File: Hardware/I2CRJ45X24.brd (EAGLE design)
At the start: 216 x 50 mm, 127 parts, among them IC1 MCP23017SO, IC2 MCP23017SO, IC3 MCP23017SO, IC4 MCP23017SO, IC5 MCP23017SO, IC6 MCP23017SO, J1 RJ45-X8, J2 RJ45-X8, J3 RJ45-X8, J4 I2C-BREAKOUT, J5 M01-PLAIN, J9 I2C-BREAKOUT

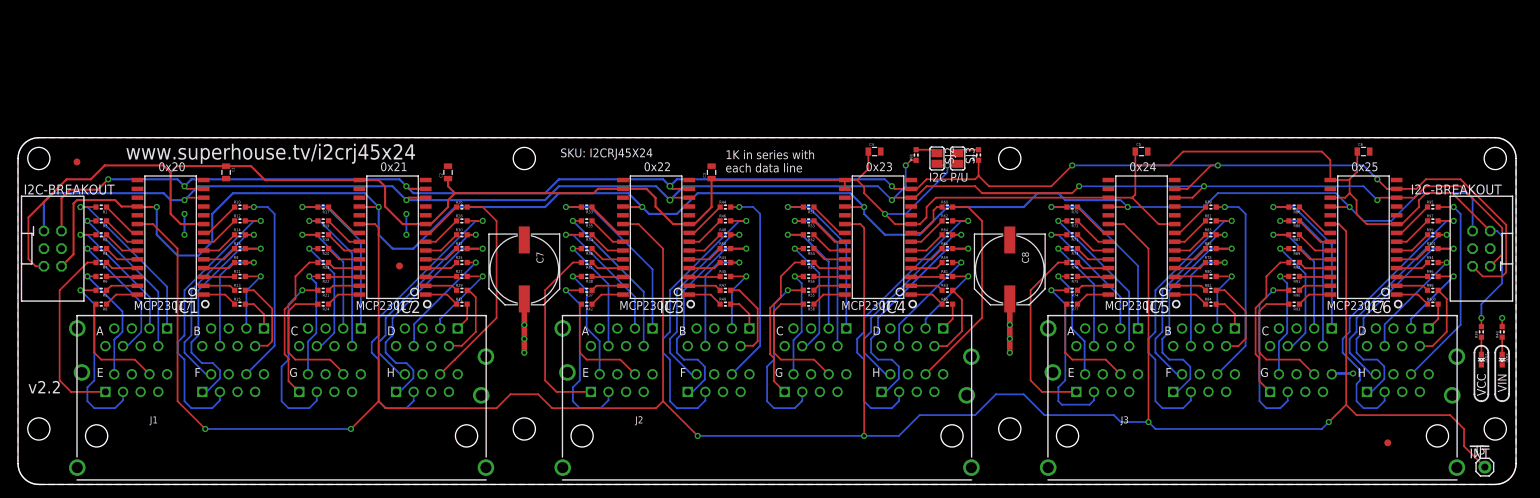
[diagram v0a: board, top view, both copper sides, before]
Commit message: Renumbered parts to optimise production.
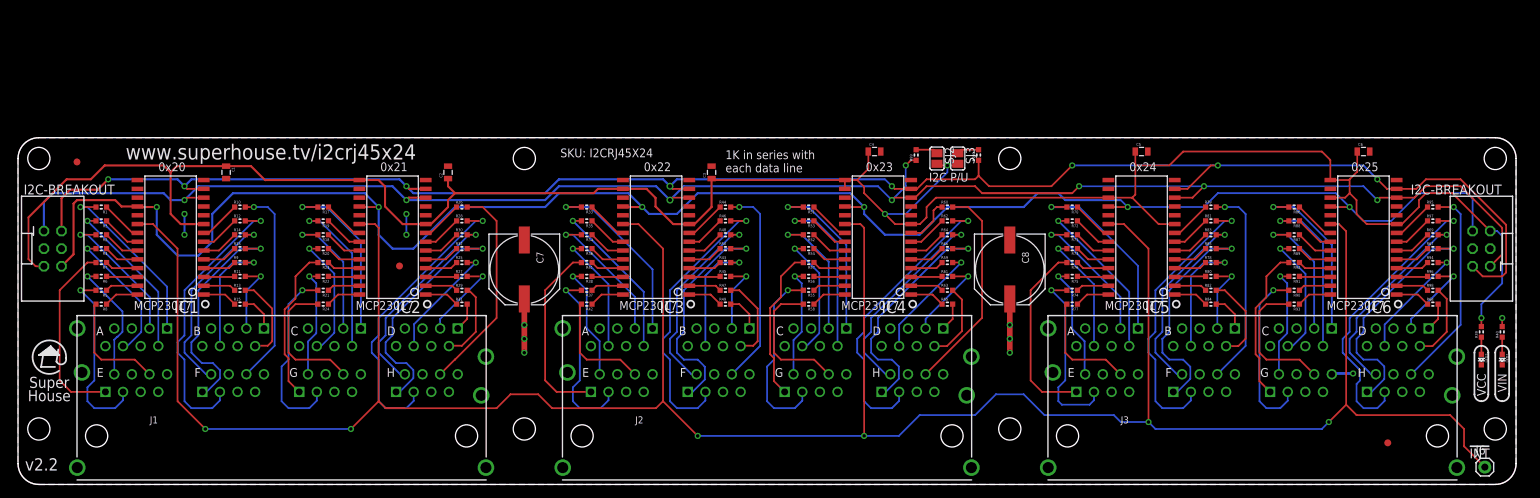
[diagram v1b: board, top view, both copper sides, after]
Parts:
- removed J9: I2C-BREAKOUT, SuperHouse-Connectors:2X03-SHROUDED
- added J6: M01-PLAIN, SuperHouse-Connectors:1X01
- J5: value M01-PLAIN -> I2C-BREAKOUT; device SuperHouse-Connectors:1X01 -> SuperHouse-Connectors:2X03-SHROUDED
- R100, R99: value 1K -> 4K7
- R68, R69: value 4K7 -> 1K
- moved R68 77.5 mm to (204.0, 26.0), turned to 0 degrees
- moved R99 75.4 mm to (129.5, 47.5), turned to 90 degrees
- moved R100 68.9 mm to (138.5, 47.5), turned to 90 degrees
- moved R69 66.5 mm to (204.0, 36.0), turned to 0 degrees
- moved J5 31.5 mm to (211.0, 34.0), turned to 180 degrees
- renumbered LED3 to LED1, R101 to R67
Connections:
- net !INT: now also J6.1; no longer J5.1
- net !RESET: now also J5.6; no longer J9.6
- net 3D1: now also R68.2; no longer R100.2
- net 3H2: now also R69.2; no longer R99.2
- net GND: now also J5.4; no longer J9.4
- net GPB0-6: now also R68.1; no longer R100.1
- net GPB5-6: now also R69.1; no longer R99.1
- net N$1: now also R99.2; no longer R68.2
- net N$2: now also R100.2; no longer R69.2
- net SCL: now also J5.1, R99.1; no longer J9.1, R68.1
- net SDA: now also J5.2, R100.1; no longer J9.2, R69.1
- net VCC: now also J5.5; no longer J9.5
- net VIN: now also J5.3; no longer J9.3
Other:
- board text added: "24-Channel I2C RJ45 Breakout"
- board text removed: "24 Channel I2C RJ45 Breakout"

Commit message: Major clean-up in preparation for recreating x8 and x16 versions based on the x24 version. Moved rear silkscreen into left third. Increased size of all data traces. Improved bottom power plane pour. Changed LED resistors to 4K7.
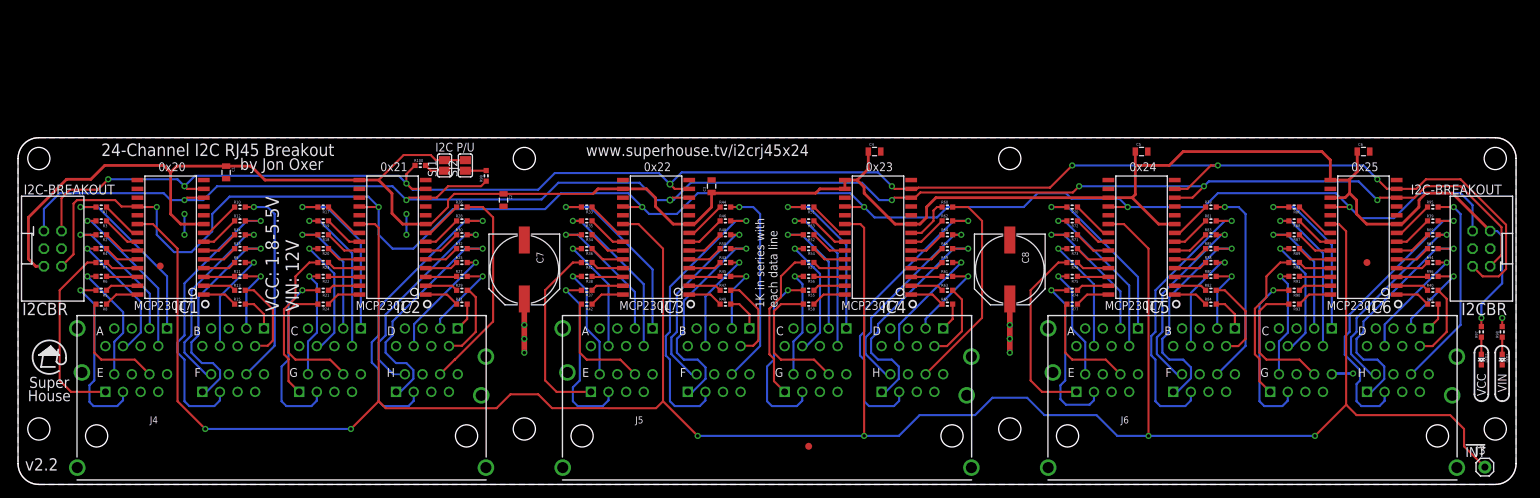
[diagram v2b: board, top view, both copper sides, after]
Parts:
- removed SJ3: SDA PU, SuperHouse-Jumpers:SJ
- added SJ1: SDA PU, SuperHouse-Jumpers:SJ
- J1, J2: value RJ45-X8 -> I2C-BREAKOUT; device SuperHouse-Connectors:RJ45-2X4 -> SuperHouse-Connectors:2X03-SHROUDED
- J3: value RJ45-X8 -> M01-PLAIN; device SuperHouse-Connectors:RJ45-2X4 -> SuperHouse-Connectors:1X01
- J4, J5: value I2C-BREAKOUT -> RJ45-X8; device SuperHouse-Connectors:2X03-SHROUDED -> SuperHouse-Connectors:RJ45-2X4
- J6: value M01-PLAIN -> RJ45-X8; device SuperHouse-Connectors:1X01 -> SuperHouse-Connectors:RJ45-2X4
- R39, R40: value 2K2 -> 1K
- R97, R98: value 1K -> 4K7
- moved J2 106.5 mm to (211.0, 34.0), turned to 180 degrees
- moved J5 106.5 mm to (108.0, 7.00), turned to 0 degrees
- moved R100 80.5 mm to (58.0, 46.0), turned to 0 degrees
- moved SJ2 68.0 mm to (64.5, 46.0), turned to 90 degrees
- moved FID3 64.5 mm to (114.0, 5.50)
- moved R99 62.1 mm to (67.5, 44.5)
- moved J1 42.6 mm to (5.00, 34.0)
- moved J4 42.6 mm to (38.0, 7.00)
- moved J3 33.8 mm to (211.5, 2.50)
- moved J6 33.8 mm to (178.0, 7.00)
- moved FID2 26.2 mm to (194.5, 32.0)
- moved FID1 19.2 mm to (20.5, 31.5)
- moved R39 17.5 mm to (204.0, 38.0), turned to 0 degrees
- moved R97 17.5 mm to (211.0, 22.0), turned to 90 degrees
- moved R40 11.7 mm to (204.0, 28.0), turned to 0 degrees
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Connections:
- net !INT: now also J3.1; no longer J6.1
- net !RESET: now also J1.6, J2.6; no longer J4.6, J5.6
- net 1A1: now also J4.A1; no longer J1.A1
- net 1A2: now also J4.A2; no longer J1.A2
- net 1A3: now also J4.A3; no longer J1.A3
- net 1A6: now also J4.A6; no longer J1.A6
- net 1B1: now also J4.B1; no longer J1.B1
- net 1B2: now also J4.B2; no longer J1.B2
- net 1B3: now also J4.B3; no longer J1.B3
- net 1B6: now also J4.B6; no longer J1.B6
- net 1C1: now also J4.C1; no longer J1.C1
- net 1C2: now also J4.C2; no longer J1.C2
- net 1C3: now also J4.C3; no longer J1.C3
- net 1C6: now also J4.C6; no longer J1.C6
- net 1D1: now also J4.D1; no longer J1.D1
- net 1D2: now also J4.D2; no longer J1.D2
- net 1D3: now also J4.D3; no longer J1.D3
- net 1D6: now also J4.D6; no longer J1.D6
- net 1E1: now also J4.E1; no longer J1.E1
- net 1E2: now also J4.E2; no longer J1.E2
- net 1E3: now also J4.E3; no longer J1.E3
- net 1E6: now also J4.E6; no longer J1.E6
- net 1F1: now also J4.F1; no longer J1.F1
- net 1F2: now also J4.F2; no longer J1.F2
- net 1F3: now also J4.F3; no longer J1.F3
- net 1F6: now also J4.F6; no longer J1.F6
- net 1G1: now also J4.G1; no longer J1.G1
- net 1G2: now also J4.G2; no longer J1.G2
- net 1G3: now also J4.G3; no longer J1.G3
- net 1G6: now also J4.G6; no longer J1.G6
- net 1H1: now also J4.H1; no longer J1.H1
- net 1H2: now also J4.H2; no longer J1.H2
- net 1H3: now also J4.H3; no longer J1.H3
- net 1H6: now also J4.H6; no longer J1.H6
- net 2A1: now also J5.A1; no longer J2.A1
- net 2A2: now also J5.A2; no longer J2.A2
- net 2A3: now also J5.A3; no longer J2.A3
- net 2A6: now also J5.A6; no longer J2.A6
- net 2B1: now also J5.B1; no longer J2.B1
- net 2B2: now also J5.B2; no longer J2.B2
- net 2B3: now also J5.B3; no longer J2.B3
- net 2B6: now also J5.B6; no longer J2.B6
- net 2C1: now also J5.C1; no longer J2.C1
- net 2C2: now also J5.C2; no longer J2.C2
- net 2C3: now also J5.C3; no longer J2.C3
- net 2C6: now also J5.C6; no longer J2.C6
- net 2D1: now also J5.D1; no longer J2.D1
- net 2D2: now also J5.D2; no longer J2.D2
- net 2D3: now also J5.D3; no longer J2.D3
- net 2D6: now also J5.D6; no longer J2.D6
- net 2E1: now also J5.E1; no longer J2.E1
- net 2E2: now also J5.E2; no longer J2.E2
- net 2E3: now also J5.E3; no longer J2.E3
- net 2E6: now also J5.E6; no longer J2.E6
- net 2F1: now also J5.F1; no longer J2.F1
- net 2F2: now also J5.F2; no longer J2.F2
- net 2F3: now also J5.F3; no longer J2.F3
- net 2F6: now also J5.F6; no longer J2.F6
- net 2G1: now also J5.G1; no longer J2.G1
- net 2G2: now also J5.G2; no longer J2.G2
- net 2G3: now also J5.G3; no longer J2.G3
- net 2G6: now also J5.G6; no longer J2.G6
- net 2H1: now also J5.H1; no longer J2.H1
- net 2H2: now also J5.H2; no longer J2.H2
- net 2H3: now also J5.H3; no longer J2.H3
- net 2H6: now also J5.H6; no longer J2.H6
- net 3A1: now also J6.A1; no longer J3.A1
- net 3A2: now also J6.A2; no longer J3.A2
- net 3A3: now also J6.A3; no longer J3.A3
- net 3A6: now also J6.A6; no longer J3.A6
- net 3B1: now also J6.B1; no longer J3.B1
- net 3B2: now also J6.B2; no longer J3.B2
- net 3B3: now also J6.B3; no longer J3.B3
- net 3B6: now also J6.B6; no longer J3.B6
- net 3C1: now also J6.C1; no longer J3.C1
- net 3C2: now also J6.C2; no longer J3.C2
- net 3C3: now also J6.C3; no longer J3.C3
- net 3C6: now also J6.C6; no longer J3.C6
- net 3D1: now also J6.D1; no longer J3.D1
- net 3D2: now also J6.D2, R40.2; no longer J3.D2, R98.2
- net 3D3: now also J6.D3; no longer J3.D3
- net 3D6: now also J6.D6; no longer J3.D6
- net 3E1: now also J6.E1; no longer J3.E1
- net 3E2: now also J6.E2; no longer J3.E2
- net 3E3: now also J6.E3; no longer J3.E3
- net 3E6: now also J6.E6; no longer J3.E6
- net 3F1: now also J6.F1; no longer J3.F1
- net 3F2: now also J6.F2; no longer J3.F2
- net 3F3: now also J6.F3; no longer J3.F3
- net 3F6: now also J6.F6; no longer J3.F6
- net 3G1: now also J6.G1; no longer J3.G1
- net 3G2: now also J6.G2; no longer J3.G2
- net 3G3: now also J6.G3; no longer J3.G3
- net 3G6: now also J6.G6; no longer J3.G6
- net 3H1: now also J6.H1; no longer J3.H1
- net 3H2: now also J6.H2; no longer J3.H2
- net 3H3: now also J6.H3, R39.2; no longer J3.H3, R97.2
- net 3H6: now also J6.H6; no longer J3.H6
- net GND: now also J1.4, J2.4, J4.A7, J4.A8, J4.B7, J4.B8, J4.C7, J4.C8, J4.D7, J4.D8, J4.E7, J4.E8, J4.F7, J4.F8, J4.G7, J4.G8, J4.GND0, J4.GND1, J4.GND2, J4.GND3, J4.GND4, J4.GND5, J4.H7, J4.H8, J5.A7, J5.A8, J5.B7, J5.B8, J5.C7, J5.C8, J5.D7, J5.D8, J5.E7, J5.E8, J5.F7, J5.F8, J5.G7, J5.G8, J5.GND0, J5.GND1, J5.GND2, J5.GND3, J5.GND4, J5.GND5, J5.H7, J5.H8, J6.A7, J6.A8, J6.B7, J6.B8, J6.C7, J6.C8, J6.D7, J6.D8, J6.E7, J6.E8, J6.F7, J6.F8, J6.G7, J6.G8, J6.GND0, J6.GND1, J6.GND2, J6.GND3, J6.GND4, J6.GND5, J6.H7, J6.H8; no longer J1.A7, J1.A8, J1.B7, J1.B8, J1.C7, J1.C8, J1.D7, J1.D8, J1.E7, J1.E8, J1.F7, J1.F8, J1.G7, J1.G8, J1.GND0, J1.GND1, J1.GND2, J1.GND3, J1.GND4, J1.GND5, J1.H7, J1.H8, J2.A7, J2.A8, J2.B7, J2.B8, J2.C7, J2.C8, J2.D7, J2.D8, J2.E7, J2.E8, J2.F7, J2.F8, J2.G7, J2.G8, J2.GND0, J2.GND1, J2.GND2, J2.GND3, J2.GND4, J2.GND5, J2.H7, J2.H8, J3.A7, J3.A8, J3.B7, J3.B8, J3.C7, J3.C8, J3.D7, J3.D8, J3.E7, J3.E8, J3.F7, J3.F8, J3.G7, J3.G8, J3.GND0, J3.GND1, J3.GND2, J3.GND3, J3.GND4, J3.GND5, J3.H7, J3.H8, J4.4, J5.4
- net GPB1-6: now also R40.1; no longer R98.1
- net GPB6-6: now also R39.1; no longer R97.1
- net N$2: now also SJ1.1; no longer SJ3.1
- net N$7: now also R97.1; no longer R39.1
- net N$8: now also R98.1; no longer R40.1
- net SCL: now also J1.1, J2.1; no longer J4.1, J5.1
- net SDA: now also J1.2, J2.2; no longer J4.2, J5.2
- net VCC: now also J1.5, J2.5, R97.2, SJ1.2; no longer J4.5, J5.5, R39.2, SJ3.2
- net VIN: now also J1.3, J2.3, J4.A4, J4.A5, J4.B4, J4.B5, J4.C4, J4.C5, J4.D4, J4.D5, J4.E4, J4.E5, J4.F4, J4.F5, J4.G4, J4.G5, J4.H4, J4.H5, J5.A4, J5.A5, J5.B4, J5.B5, J5.C4, J5.C5, J5.D4, J5.D5, J5.E4, J5.E5, J5.F4, J5.F5, J5.G4, J5.G5, J5.H4, J5.H5, J6.A4, J6.A5, J6.B4, J6.B5, J6.C4, J6.C5, J6.D4, J6.D5, J6.E4, J6.E5, J6.F4, J6.F5, J6.G4, J6.G5, J6.H4, J6.H5, R98.2; no longer J1.A4, J1.A5, J1.B4, J1.B5, J1.C4, J1.C5, J1.D4, J1.D5, J1.E4, J1.E5, J1.F4, J1.F5, J1.G4, J1.G5, J1.H4, J1.H5, J2.A4, J2.A5, J2.B4, J2.B5, J2.C4, J2.C5, J2.D4, J2.D5, J2.E4, J2.E5, J2.F4, J2.F5, J2.G4, J2.G5, J2.H4, J2.H5, J3.A4, J3.A5, J3.B4, J3.B5, J3.C4, J3.C5, J3.D4, J3.D5, J3.E4, J3.E5, J3.F4, J3.F5, J3.G4, J3.G5, J3.H4, J3.H5, J4.3, J5.3, R40.2
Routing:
- net VCC: track 332.3 -> 326.7 mm, vias 3 -> 1
- net !RESET: track 264.5 -> 259.2 mm
- net !INT: track 387.0 -> 389.4 mm
- net SCL: track 253.7 -> 255.7 mm, vias 8 -> 7
- net 2B6: track 17.1 -> 15.3 mm
- net 1B6: track 17.1 -> 15.3 mm
- net 3B6: track 17.1 -> 15.6 mm
- net SDA: track 256.6 -> 257.5 mm
- net 3A1: track 27.3 -> 26.3 mm
- net 3C2: track 23.6 -> 22.7 mm
- net 2C2: track 23.6 -> 22.7 mm
- net 1A1: track 25.5 -> 26.4 mm
- net 1H2: track 29.7 -> 30.6 mm
- net 2F1: track 33.0 -> 32.2 mm
- net 2A2: track 23.5 -> 24.2 mm
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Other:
- board text added: "I2CBR"
- board text added: "VCC: 1.8-5.5V VIN: 12V"

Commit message: Added weak pull-up on RESET line.
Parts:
- added R101: 22K, SuperHouse-DiscreteSemi:R0603
- added SJ3: RST-PU, SuperHouse-Jumpers:SJC
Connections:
- new net N$3: R101.2, SJ3.1
- net !RESET: now also R101.1
- net VCC: now also SJ3.2
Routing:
- net N$3: track 0.00 -> 35.8 mm, vias 0 -> 2
- net !RESET: track 259.2 -> 268.4 mm
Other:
- board text added: "RST P/U"
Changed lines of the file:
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@@
 <setting verticaltext="up"/>
 </settings>
-<grid distance="0.1" unitdist="mm" unit="mm" style="lines" multiple="1" display="yes" altdistance="0.005" altunitdist="inch" altunit="inch"/>
+<grid distance="1" unitdist="mm" unit="mm" style="lines" multiple="1" display="yes" altdistance="0.005" altunitdist="inch" altunit="inch"/>
 <layers>
 <layer number="1" name="Top" color="4" fill="1" visible="yes" active="yes"/>
@@
 </layers>
 <board>
-<fusionsync huburn="a.cGVyc29uYWw6dWUyZDliZmNi" projecturn="a.cGVyc29uYWw6dWUyZDliZmNiIzIwMTkwNjE5MTk5NjgzNjgx" f3durn="urn:adsk.wipprod:dm.lineage:7PE12rU6Rs2d8xNWJ3I8mw" pcbguid="240f1cde-c83f-4e3e-9fac-562d2bf45fdf" lastpulledtime="" lastsyncedchangeguid="1491f9b9-a179-9c0a-9821-19275fe4b9b0" latestrevisionid="" lastsyncedrevisionid="" lastboardhashguid="1feeb865-bf47-de78-9034-8c028aa0d644" lastpushedtime="2021-04-15T02:54:13Z" linktopcb3d="false"/>
+<fusionsync huburn="a.cGVyc29uYWw6dWUyZDliZmNi" projecturn="a.cGVyc29uYWw6dWUyZDliZmNiIzIwMTkwNjE5MTk5NjgzNjgx" f3durn="urn:adsk.wipprod:dm.lineage:7PE12rU6Rs2d8xNWJ3I8mw" pcbguid="240f1cde-c83f-4e3e-9fac-562d2bf45fdf" lastpulledtime="" lastsyncedchangeguid="1491f9b9-a179-9c0a-9821-19275fe4b9b0" latestrevisionid="" lastsyncedrevisionid="" lastboardhashguid="57911f44-b240-5674-ec1f-8acbffdfcb08" lastpushedtime="2021-04-15T04:03:47Z" linktopcb3d="false"/>
 <plain>
 <wire x1="3" y1="0" x2="0" y2="3" width="0" layer="20" curve="-90"/>
@@
 <circle x="3" y="47" radius="3.201559375" width="0.254" layer="41"/>
 <circle x="3" y="47" radius="3.201559375" width="0.254" layer="42"/>
-<dimension x1="0" y1="-1" x2="38" y2="-1" x3="19" y3="-9" textsize="1.778" layer="47"/>
-<dimension x1="38" y1="-1" x2="108" y2="-1" x3="73" y3="-9" textsize="1.778" layer="47"/>
-<dimension x1="108" y1="-1" x2="178" y2="-1" x3="143" y3="-9" textsize="1.778" layer="47"/>
+<dimension x1="0" y1="-1" x2="38" y2="-1" x3="19" y3="-7" textsize="1.778" layer="47"/>
+<dimension x1="38" y1="-1" x2="108" y2="-1" x3="73" y3="-7" textsize="1.778" layer="47"/>
+<dimension x1="108" y1="-1" x2="178" y2="-1" x3="143" y3="-7" textsize="1.778" layer="47"/>
 <text x="47.5" y="37.354" size="1.6764" layer="22" font="vector" ratio="17" rot="MR0" align="bottom-center">www.superhouse.tv</text>
 <dimension x1="3" y1="51" x2="73" y2="51" x3="38" y3="52" textsize="1.778" layer="47"/>
@@
 <text x="37.455" y="1.854" size="2.3" layer="22" font="vector" ratio="17" rot="MR0" align="bottom-center">www.superhouse.tv/i2crj45x24</text>
 <text x="4.671" y="11.309" size="1.4224" layer="22" font="vector" ratio="17" rot="MR90">SKU: I2CRJ45X24</text>
+<text x="8.691" y="43.671" size="1.27" layer="21" font="vector" ratio="17" align="bottom-center">RST P/U</text>
+<dimension x1="217" y1="50" x2="217" y2="0" x3="220" y3="25" textsize="1.778" layer="47"/>
+<dimension x1="0" y1="57" x2="216" y2="57" x3="108" y3="58" textsize="1.778" layer="47"/>
+<dimension x1="178" y1="-1" x2="216" y2="-1" x3="197" y3="-7" textsize="1.778" layer="47"/>
 </plain>
 <attributes>
@@
 <attribute name="VALUE" x="214.9652" y="20.984" size="0.4064" layer="27" font="vector" rot="R90"/>
 </element>
+<element name="R101" library="SuperHouse-DiscreteSemi" library_urn="urn:adsk.eagle:library:11768461" package="R0603" package3d_urn="urn:adsk.eagle:package:11768543/2" value="22K" x="3.6" y="23.1" smashed="yes" rot="R180">
+<attribute name="NAME" x="4.489" y="22.592" size="0.4064" layer="25" font="vector" rot="R180"/>
+<attribute name="VALUE" x="4.616" y="24.0652" size="0.4064" layer="27" font="vector" rot="R180"/>
+</element>
+<element name="SJ3" library="SuperHouse-Jumpers" library_urn="urn:adsk.eagle:library:12190622" package="SJC" package3d_urn="urn:adsk.eagle:package:7066342/2" value="RST-PU" x="8.4" y="46.9" smashed="yes" rot="R270">
+<attribute name="NAME" x="9.543" y="48.551" size="1.27" layer="25" ratio="10" rot="R270"/>
+<attribute name="VALUE" x="8.4" y="46.4999" size="0.02" layer="27" rot="R270"/>
+</element>
 </elements>
 <signals>
@@
 <via x="13" y="44" extent="1-16" drill="0.5"/>
 <wire x1="13" y1="44" x2="11.5" y2="42.5" width="0.3048" layer="1"/>
-<wire x1="11.5" y1="42.5" x2="7.5" y2="42.5" width="0.3048" layer="1"/>
-<wire x1="7.5" y1="42.5" x2="6.27" y2="41.27" width="0.3048" layer="1"/>
-<wire x1="6.27" y1="41.27" x2="6.27" y2="36.54" width="0.3048" layer="1"/>
+<wire x1="11.5" y1="42.5" x2="8" y2="42.5" width="0.3048" layer="1"/>
+<wire x1="8" y1="42.5" x2="6.27" y2="40.77" width="0.3048" layer="1"/>
+<wire x1="6.27" y1="40.77" x2="6.27" y2="36.54" width="0.3048" layer="1"/>
 <wire x1="172" y1="46" x2="173" y2="46" width="0.3048" layer="1"/>
 <wire x1="168.62" y1="42.62" x2="172" y2="46" width="0.3048" layer="1"/>
@@
 <wire x1="2.54" y1="31.46" x2="1.5" y2="32.5" width="0.4064" layer="1"/>
 <wire x1="1.5" y1="32.5" x2="1.5" y2="38.5" width="0.4064" layer="1"/>
-<wire x1="1.5" y1="38.5" x2="7" y2="44" width="0.4064" layer="1"/>
-<wire x1="7" y1="44" x2="10.5" y2="44" width="0.4064" layer="1"/>
-<wire x1="10.5" y1="44" x2="12.5" y2="46" width="0.4064" layer="1"/>
 <wire x1="21" y1="46" x2="22" y2="45" width="0.4064" layer="1"/>
-<wire x1="12.5" y1="46" x2="21" y2="46" width="0.4064" layer="1"/>
+<wire x1="21" y1="46" x2="8.538" y2="46" width="0.4064" layer="1"/>
 <wire x1="100" y1="40" x2="100" y2="42.1" width="0.4064" layer="1"/>
 <wire x1="100" y1="42.1" x2="100.1" y2="42" width="0.4064" layer="1"/>
@@
 <wire x1="55.6" y1="47.5" x2="51.99" y2="43.89" width="0.3048" layer="1"/>
 <wire x1="59.5" y1="47.5" x2="55.6" y2="47.5" width="0.3048" layer="1"/>
+<contactref element="SJ3" pad="2"/>
+<wire x1="8.538" y1="46" x2="8.4" y2="46.138" width="0.4064" layer="1"/>
+<wire x1="8.538" y1="45.538" x2="8.538" y2="46" width="0.4064" layer="1"/>
+<wire x1="1.5" y1="38.5" x2="8.538" y2="45.538" width="0.4064" layer="1"/>
 </signal>
 <signal name="!INT">
@@
 <wire x1="14" y1="41" x2="8.5" y2="41" width="0.3048" layer="1"/>
 <wire x1="8" y1="40.5" x2="8" y2="33.19" width="0.3048" layer="1"/>
+<contactref element="R101" pad="1"/>
+<wire x1="4.362" y1="23.1" x2="4.362" y2="28.552" width="0.3048" layer="1"/>
+<wire x1="6.27" y1="30.46" x2="4.362" y2="28.552" width="0.3048" layer="1"/>
+<wire x1="6.27" y1="30.46" x2="6.27" y2="31.46" width="0.3048" layer="1"/>
 </signal>
 <signal name="N$7">
@@
 <wire x1="214" y1="21.238" x2="214" y2="18.762" width="0.3048" layer="1"/>
 </signal>
+<signal name="N$3">
+<contactref element="R101" pad="2"/>
+<contactref element="SJ3" pad="1"/>
+<wire x1="2.838" y1="23.1" x2="2.838" y2="21.838" width="0.3048" layer="1"/>
+<wire x1="2.838" y1="21.838" x2="2.5" y2="21.5" width="0.3048" layer="1"/>
+<via x="2.5" y="21.5" extent="1-16" drill="0.5"/>
+<wire x1="2.5" y1="21.5" x2="1.5" y2="22.5" width="0.3048" layer="16"/>
+<wire x1="6" y1="44" x2="8" y2="44" width="0.3048" layer="16"/>
+<wire x1="8" y1="44" x2="10.5" y2="46.5" width="0.3048" layer="16"/>
+<wire x1="10.5" y1="46.5" x2="10.5" y2="48" width="0.3048" layer="16"/>
+<via x="10.5" y="48" extent="1-16" drill="0.5"/>
+<wire x1="10.5" y1="48" x2="10.1620125" y2="47.662" width="0.3048" layer="1"/>
+<wire x1="10.1620125" y1="47.662" x2="8.4" y2="47.662" width="0.3048" layer="1"/>
+<wire x1="1.5" y1="22.5" x2="1.5" y2="39.5" width="0.3048" layer="16"/>
+<wire x1="1.5" y1="39.5" x2="6" y2="44" width="0.3048" layer="16"/>
+</signal>
 </signals>
 <mfgpreviewcolors>
@@
 <mfgpreviewcolor name="substratecolor" color="0xFF786E46"/>
 </mfgpreviewcolors>
+<errors>
+</errors>
 </board>
 </drawing>

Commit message: Bumped version to v3.0 for release.
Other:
- board text added: "v3.0"
- board text removed: "v2.2"
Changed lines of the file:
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@@
 <wire x1="216" y1="3" x2="213" y2="0" width="0" layer="20" curve="-90"/>
 <wire x1="213" y1="0" x2="3" y2="0" width="0" layer="20"/>
-<text x="1" y="2" size="1.778" layer="21" font="vector" ratio="17">v2.2</text>
+<text x="1" y="2" size="1.9" layer="21" font="vector" ratio="17">v3.0</text>
 <text x="97.955" y="47.354" size="1.6764" layer="21" font="vector" ratio="17" align="bottom-center">www.superhouse.tv/i2crj45x24</text>
 <hole x="143" y="8" drill="3.2"/>
